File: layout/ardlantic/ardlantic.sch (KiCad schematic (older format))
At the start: 13 parts, among them J1 PowerSupply, J2 OnOffSensor, J3 IR Input, J4 Shield NRF24 Input, J5 Shield NRF24 PowerSupply, J6 Shield NRF24 Output, J7 Temp Input, U1 Arduino Pro Micro

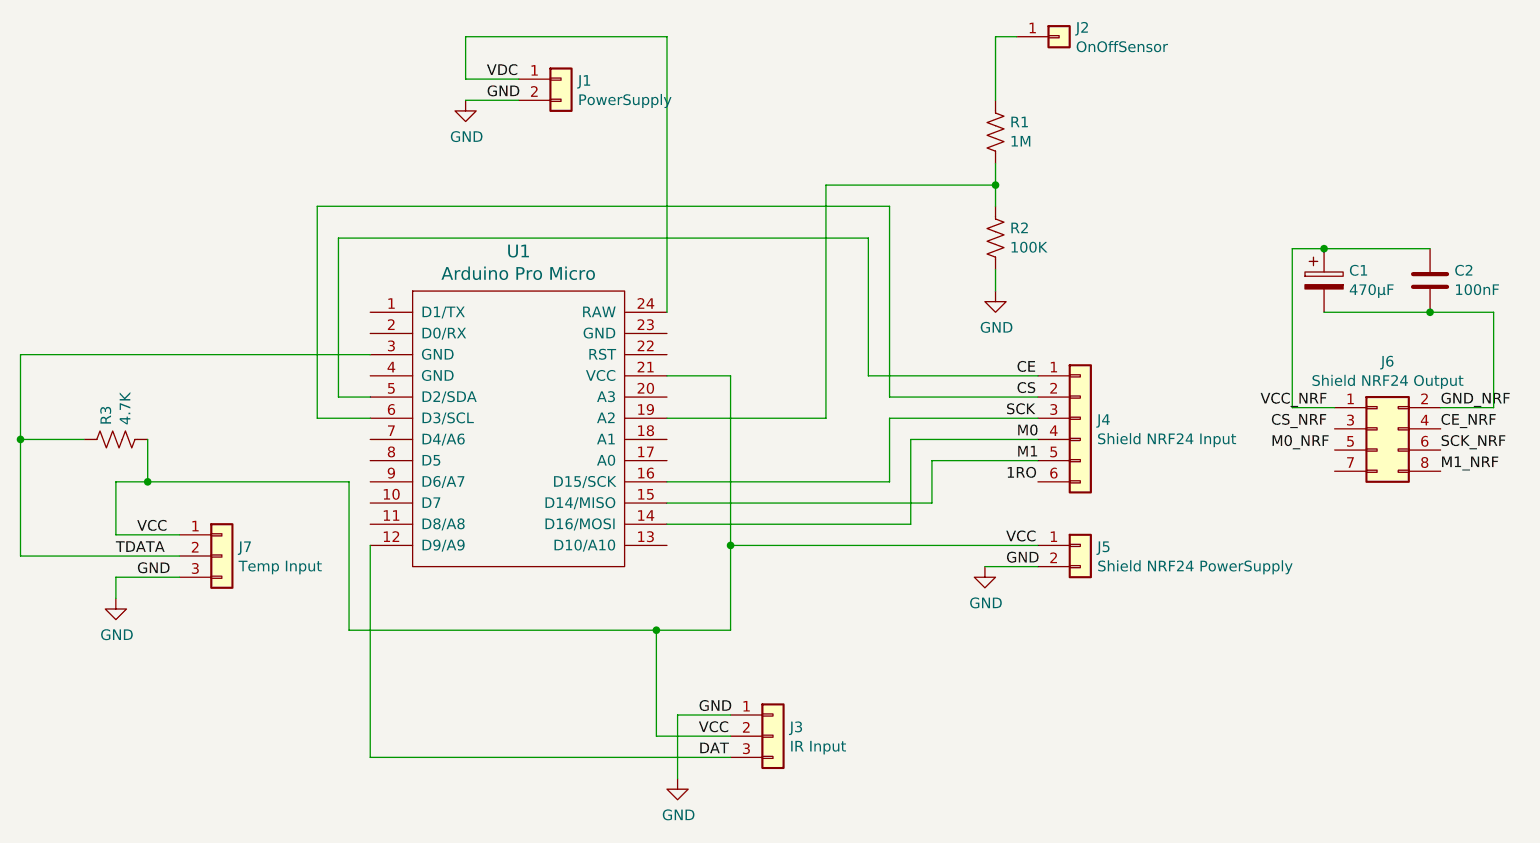
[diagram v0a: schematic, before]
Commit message: New layout revision with fix + fix mysensor pin + add temperature sensor
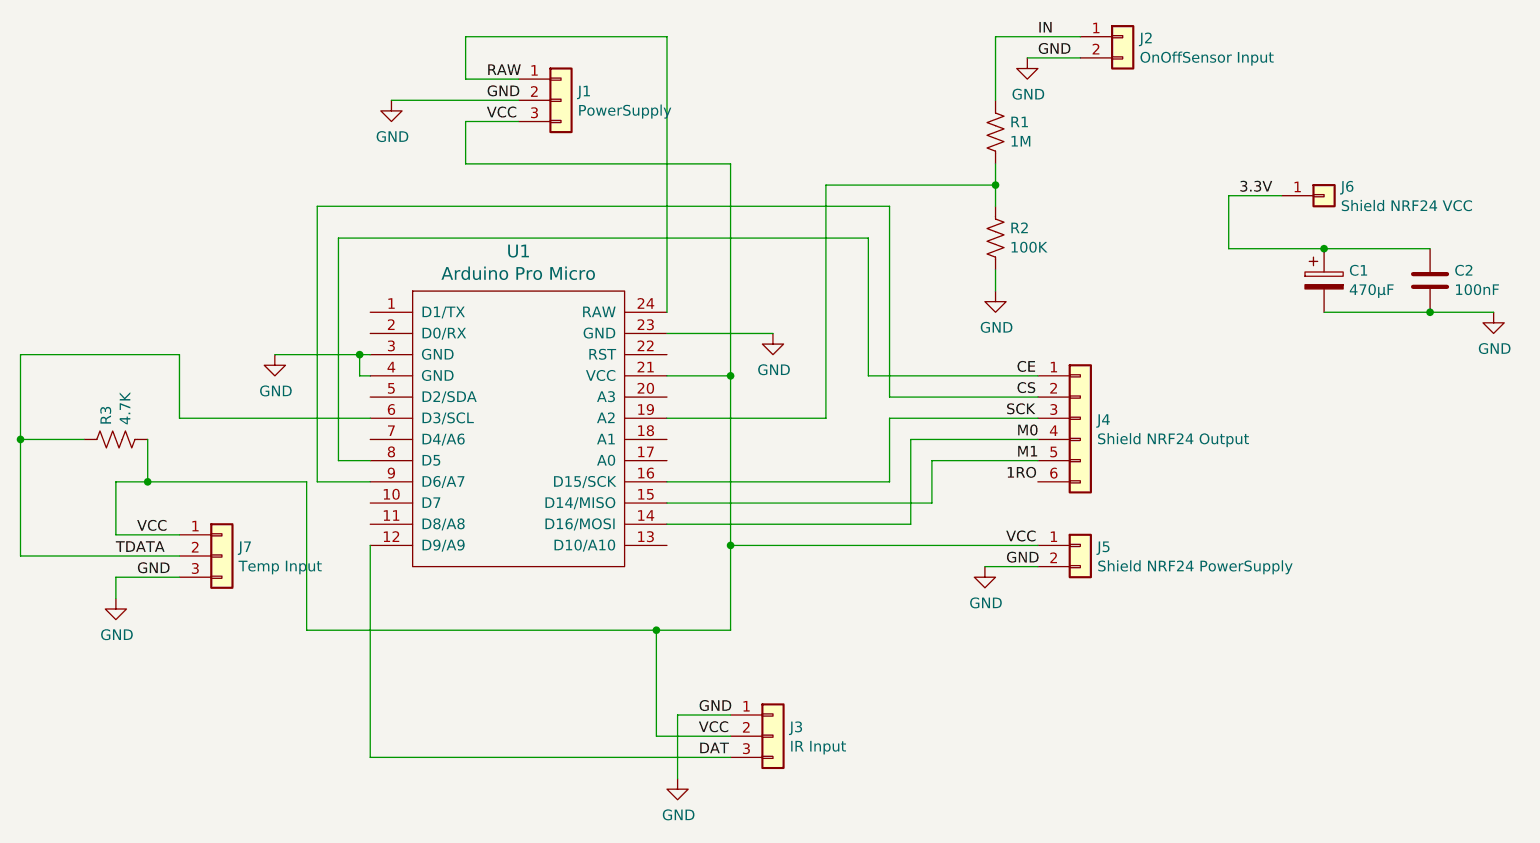
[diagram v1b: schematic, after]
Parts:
- removed J1: PowerSupply, Connector_PinHeader_2.54mm:PinHeader_1x02_P2.54mm_Vertical, symbol Connector_Generic:Conn_01x02
- removed J2: OnOffSensor, Connector_PinHeader_2.54mm:PinHeader_1x01_P2.54mm_Vertical, symbol Connector_Generic:Conn_01x01
- removed J6: Shield NRF24 Output, Connector_PinHeader_2.54mm:PinHeader_2x08_P2.54mm_Vertical, symbol Connector_Generic:Conn_02x04_Odd_Even
- added J1: PowerSupply, Connector_PinHeader_2.54mm:PinHeader_1x03_P2.54mm_Vertical, symbol Connector_Generic:Conn_01x03
- added J2: OnOffSensor Input, Connector_PinHeader_2.54mm:PinHeader_1x02_P2.54mm_Vertical, symbol Connector_Generic:Conn_01x02
- added J6: Shield NRF24 VCC, Connector_PinHeader_2.54mm:PinHeader_1x01_P2.54mm_Vertical, symbol Connector_Generic:Conn_01x01
- J4: value Shield NRF24 Input -> Shield NRF24 Output
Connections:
- net GND_NRF is gone; now on net GND: C1.2, C2.2
- net CE: now also U1.8 (D5); no longer U1.5 (D2/SDA)
- net CS: now also U1.9 (D6/A7); no longer U1.6 (D3/SCL)
- net GND: now also U1.23 (GND), U1.3 (GND), U1.4 (GND), J1.2 (Pin_2), J2.2 (Pin_2)
- net TDATA: now also U1.6 (D3/SCL); no longer U1.3 (GND)
- net VCC: now also J1.3 (Pin_3)
- net 3.3V: now reaches C1.1, C2.1
- net 3.3V: now also J6.1 (Pin_1)
- net IN: now reaches R1.1
- net IN: now also J2.1 (Pin_1)
- net VDC renamed RAW
- net RAW: now also J1.1 (Pin_1)
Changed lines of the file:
@@
 EESchema Schematic File Version 4
-LIBS:ardlantic-cache
-EELAYER 26 0
+EELAYER 30 0
 EELAYER END
 $Descr A4 11693 8268
@@
 P 7300 2700
 F 0 "J4" H 7379 2692 50  0000 L CNN
-F 1 "Shield NRF24 Input" H 7379 2601 50  0000 L CNN
+F 1 "Shield NRF24 Output" H 7379 2601 50  0000 L CNN
 F 2 "Connector_PinHeader_2.54mm:PinHeader_1x06_P2.54mm_Vertical" H 7300 2700 50  0001 C CNN
 F 3 "~" H 7300 2700 50  0001 C CNN
 	1    7300 2700
-	1    0    0    -1
-$EndComp
-$Comp
-L Connector_Generic:Conn_02x04_Odd_Even J6
-U 1 1 5C4E0E70
-P 8700 2750
-F 0 "J6" H 8750 3067 50  0000 C CNN
-F 1 "Shield NRF24 Output" H 8750 2976 50  0000 C CNN
-F 2 "Connector_PinHeader_2.54mm:PinHeader_2x08_P2.54mm_Vertical" H 8700 2750 50  0001 C CNN
-F 3 "~" H 8700 2750 50  0001 C CNN
-	1    8700 2750
 	1    0    0    -1
 $EndComp
@@
 	1    0    0    -1
 $EndComp
-$Comp
-L Connector_Generic:Conn_01x02 J1
-U 1 1 5C4E133B
-P 4850 1100
-F 0 "J1" H 4930 1092 50  0000 L CNN
-F 1 "PowerSupply" H 4930 1001 50  0000 L CNN
-F 2 "Connector_PinHeader_2.54mm:PinHeader_1x02_P2.54mm_Vertical" H 4850 1100 50  0001 C CNN
-F 3 "~" H 4850 1100 50  0001 C CNN
-	1    4850 1100
-	1    0    0    -1
-$EndComp
-$Comp
-L Connector_Generic:Conn_01x01 J2
-U 1 1 5C4E1537
-P 7200 900
-F 0 "J2" H 7279 942 50  0000 L CNN
-F 1 "OnOffSensor" H 7279 851 50  0000 L CNN
-F 2 "Connector_PinHeader_2.54mm:PinHeader_1x01_P2.54mm_Vertical" H 7200 900 50  0001 C CNN
-F 3 "~" H 7200 900 50  0001 C CNN
-	1    7200 900
-	1    0    0    -1
-$EndComp
 Wire Wire Line
 	3950 3300 3950 4300
@@
 GND
 Wire Wire Line
-	3950 2600 3800 2600
-Wire Wire Line
-	3800 2600 3800 1850
-Wire Wire Line
 	3800 1850 6300 1850
 Wire Wire Line
@@
 Text Label 7000 2500 0    50   ~ 0
 CE
-Wire Wire Line
-	3950 2700 3700 2700
-Wire Wire Line
-	3700 2700 3700 1700
 Wire Wire Line
 	3700 1700 6400 1700
@@
 Wire Wire Line
 	4400 1100 4650 1100
-Wire Wire Line
-	4400 1200 4650 1200
 Text Label 4500 1100 0    50   ~ 0
-VDC
+RAW
 Text Label 4500 1200 0    50   ~ 0
 GND
@@
 L power:GND #PWR0101
 U 1 1 5C4EA1A6
-P 4400 1200
-F 0 "#PWR0101" H 4400 950 50  0001 C CNN
-F 1 "GND" H 4405 1027 50  0000 C CNN
-F 2 "" H 4400 1200 50  0001 C CNN
-F 3 "" H 4400 1200 50  0001 C CNN
-	1    4400 1200
+P 4050 1200
+F 0 "#PWR0101" H 4050 950 50  0001 C CNN
+F 1 "GND" H 4055 1027 50  0000 C CNN
+F 2 "" H 4050 1200 50  0001 C CNN
+F 3 "" H 4050 1200 50  0001 C CNN
+	1    4050 1200
 	1    0    0    -1
 $EndComp
@@
 	6900 1200 6900 900
 Wire Wire Line
-	6900 900  7000 900
-Wire Wire Line
 	6100 2700 6100 1600
 Wire Wire Line
@@
 Wire Wire Line
 	6900 1600 6900 1700
-Text Label 8150 2650 0    50   ~ 0
-VCC_NRF
-Text Label 8200 2750 0    50   ~ 0
-CS_NRF
-Text Label 8200 2850 0    50   ~ 0
-M0_NRF
-Text Label 9000 2650 0    50   ~ 0
-GND_NRF
-Text Label 9000 2750 0    50   ~ 0
-CE_NRF
-Text Label 9000 2850 0    50   ~ 0
-SCK_NRF
-Text Label 9000 2950 0    50   ~ 0
-M1_NRF
 Text Label 6950 3000 0    50   ~ 0
 1RO
@@
 $EndComp
 Wire Wire Line
-	9250 2650 9000 2650
-Wire Wire Line
 	8450 2200 8950 2200
 Wire Wire Line
 	8450 1900 8950 1900
-Wire Wire Line
-	9250 2650 9250 2200
 Wire Wire Line
 	9250 2200 8950 2200
 Connection ~ 8950 2200
-Wire Wire Line
-	8300 1900 8450 1900
 Connection ~ 8450 1900
-Wire Wire Line
-	8300 1900 8300 2650
-Wire Wire Line
-	8300 2650 8500 2650
 $Comp
 L Device:R_US R3
@@
 TDATA
 Wire Wire Line
-	2300 2400 3950 2400
-Wire Wire Line
 	2300 2400 2300 2800
 Wire Wire Line
@@
 	2900 3000 2900 2800
 Wire Wire Line
-	2900 3000 3850 3000
-Wire Wire Line
-	3850 3000 3850 3700
-Wire Wire Line
-	3850 3700 5300 3700
+	2900 3000 3650 3000
+Wire Wire Line
+	3650 3000 3650 3700
 Connection ~ 2900 3000
 Connection ~ 5300 3700
@@
 Wire Wire Line
 	2750 3450 2750 3550
+Wire Wire Line
+	3650 3700 5300 3700
+Wire Wire Line
+	3700 3000 3950 3000
+Wire Wire Line
+	3700 1700 3700 3000
+Wire Wire Line
+	3800 2900 3950 2900
+Wire Wire Line
+	3800 1850 3800 2900
+$Comp
+L Connector_Generic:Conn_01x03 J1
+U 1 1 5E2D9EDB
+P 4850 1200
+F 0 "J1" H 4929 1242 50  0000 L CNN
+F 1 "PowerSupply" H 4929 1151 50  0000 L CNN
+F 2 "Connector_PinHeader_2.54mm:PinHeader_1x03_P2.54mm_Vertical" H 4850 1200 50  0001 C CNN
+F 3 "~" H 4850 1200 50  0001 C CNN
+	1    4850 1200
+	1    0    0    -1
+$EndComp
+Wire Wire Line
+	5650 2500 5650 1500
+Wire Wire Line
+	4400 1500 4400 1300
+Connection ~ 5650 2500
+Wire Wire Line
+	4050 1200 4650 1200
+Wire Wire Line
+	4400 1300 4650 1300
+Wire Wire Line
+	4400 1500 5650 1500
+Text Label 4500 1300 0    50   ~ 0
+VCC
+$Comp
+L Connector_Generic:Conn_01x01 J6
+U 1 1 5E2F9356
+P 8450 1650
+F 0 "J6" H 8529 1692 50  0000 L CNN
+F 1 "Shield NRF24 VCC" H 8529 1601 50  0000 L CNN
+F 2 "Connector_PinHeader_2.54mm:PinHeader_1x01_P2.54mm_Vertical" H 8450 1650 50  0001 C CNN
+F 3 "~" H 8450 1650 50  0001 C CNN
+	1    8450 1650
+	1    0    0    -1
+$EndComp
+Wire Wire Line
+	8000 1900 8000 1650
+Wire Wire Line
+	8000 1650 8250 1650
+Wire Wire Line
+	8000 1900 8450 1900
+Text Label 8050 1650 0    50   ~ 0
+3.3V
+$Comp
+L power:GND #PWR0106
+U 1 1 5E2FF971
+P 9250 2200
+F 0 "#PWR0106" H 9250 1950 50  0001 C CNN
+F 1 "GND" H 9255 2027 50  0000 C CNN
+F 2 "" H 9250 2200 50  0001 C CNN
+F 3 "" H 9250 2200 50  0001 C CNN
+	1    9250 2200
+	1    0    0    -1
+$EndComp
+$Comp
+L Connector_Generic:Conn_01x02 J2
+U 1 1 5E2FFF81
+P 7500 900
+F 0 "J2" H 7580 892 50  0000 L CNN
+F 1 "OnOffSensor Input" H 7580 801 50  0000 L CNN
+F 2 "Connector_PinHeader_2.54mm:PinHeader_1x02_P2.54mm_Vertical" H 7500 900 50  0001 C CNN
+F 3 "~" H 7500 900 50  0001 C CNN
+	1    7500 900
+	1    0    0    -1
+$EndComp
+$Comp
+L power:GND #PWR0107
+U 1 1 5E30B0C6
+P 7050 1000
+F 0 "#PWR0107" H 7050 750 50  0001 C CNN
+F 1 "GND" H 7055 827 50  0000 C CNN
+F 2 "" H 7050 1000 50  0001 C CNN
+F 3 "" H 7050 1000 50  0001 C CNN
+	1    7050 1000
+	1    0    0    -1
+$EndComp
+Wire Wire Line
+	6900 900  7300 900
+Wire Wire Line
+	7050 1000 7300 1000
+Text Label 7100 1000 0    50   ~ 0
+GND
+Text Label 7100 900  0    50   ~ 0
+IN
+$Comp
+L power:GND #PWR0108
+U 1 1 5E31054B
+P 5850 2300
+F 0 "#PWR0108" H 5850 2050 50  0001 C CNN
+F 1 "GND" H 5855 2127 50  0000 C CNN
+F 2 "" H 5850 2300 50  0001 C CNN
+F 3 "" H 5850 2300 50  0001 C CNN
+	1    5850 2300
+	1    0    0    -1
+$EndComp
+Wire Wire Line
+	5350 2300 5850 2300
+Wire Wire Line
+	3950 2500 3900 2500
+Wire Wire Line
+	3900 2500 3900 2400
+Wire Wire Line
+	3900 2400 3950 2400
+$Comp
+L power:GND #PWR?
+U 1 1 5E34E0EB
+P 3500 2400
+F 0 "#PWR?" H 3500 2150 50  0001 C CNN
+F 1 "GND" H 3505 2227 50  0000 C CNN
+F 2 "" H 3500 2400 50  0001 C CNN
+F 3 "" H 3500 2400 50  0001 C CNN
+	1    3500 2400
+	1    0    0    -1
+$EndComp
+Wire Wire Line
+	3900 2400 3500 2400
+Connection ~ 3900 2400
+Wire Wire Line
+	3950 2700 3050 2700
+Wire Wire Line
+	3050 2700 3050 2400
+Wire Wire Line
+	3050 2400 2300 2400
 $EndSCHEMATC
